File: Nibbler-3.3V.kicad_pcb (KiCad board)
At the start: 2 copper layers, 17.7 x 10.2 mm, 11 parts, among them J1 CONN_01X04, J2 +3.3, J3 GND, Q1 UM6K33N, Q2 UM6K33N

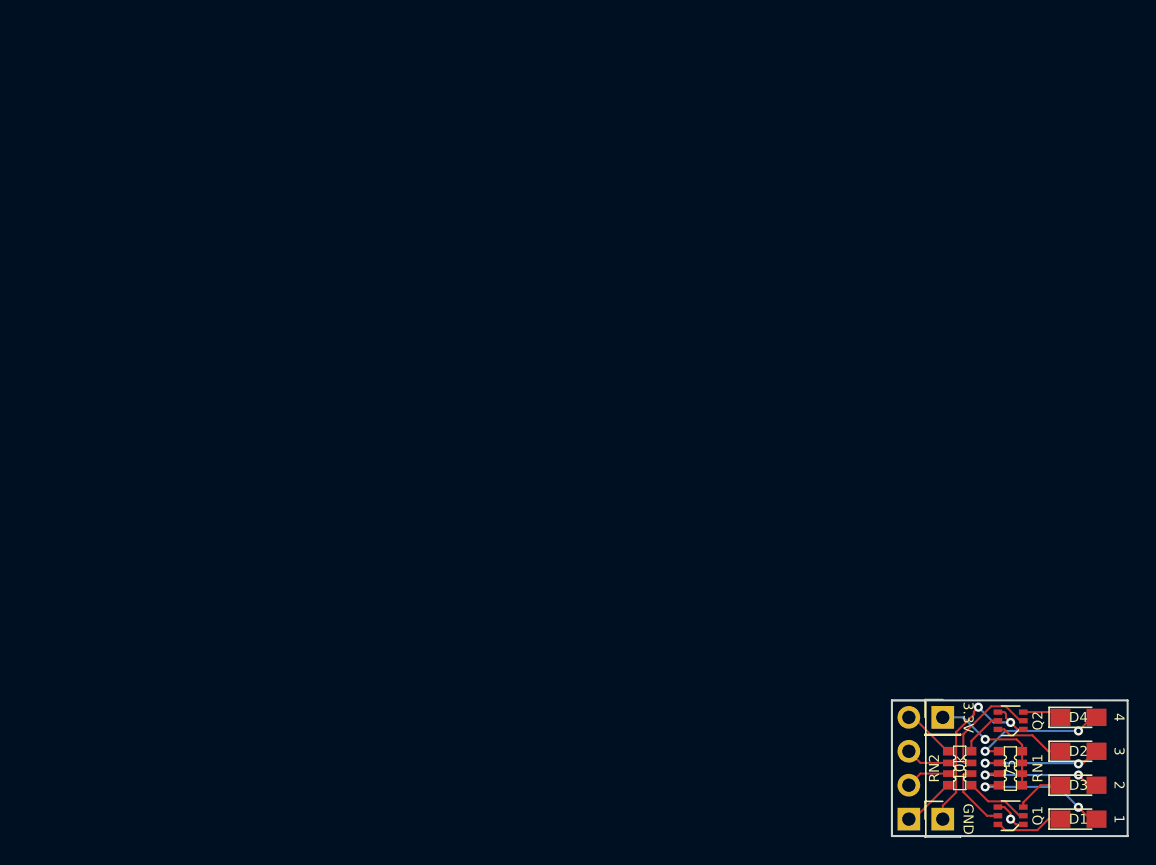
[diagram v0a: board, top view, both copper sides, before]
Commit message: Minor layout rework - rotated current limit resistor in layout and reversed LED connections in schematic. Modified bottom silkscreen text
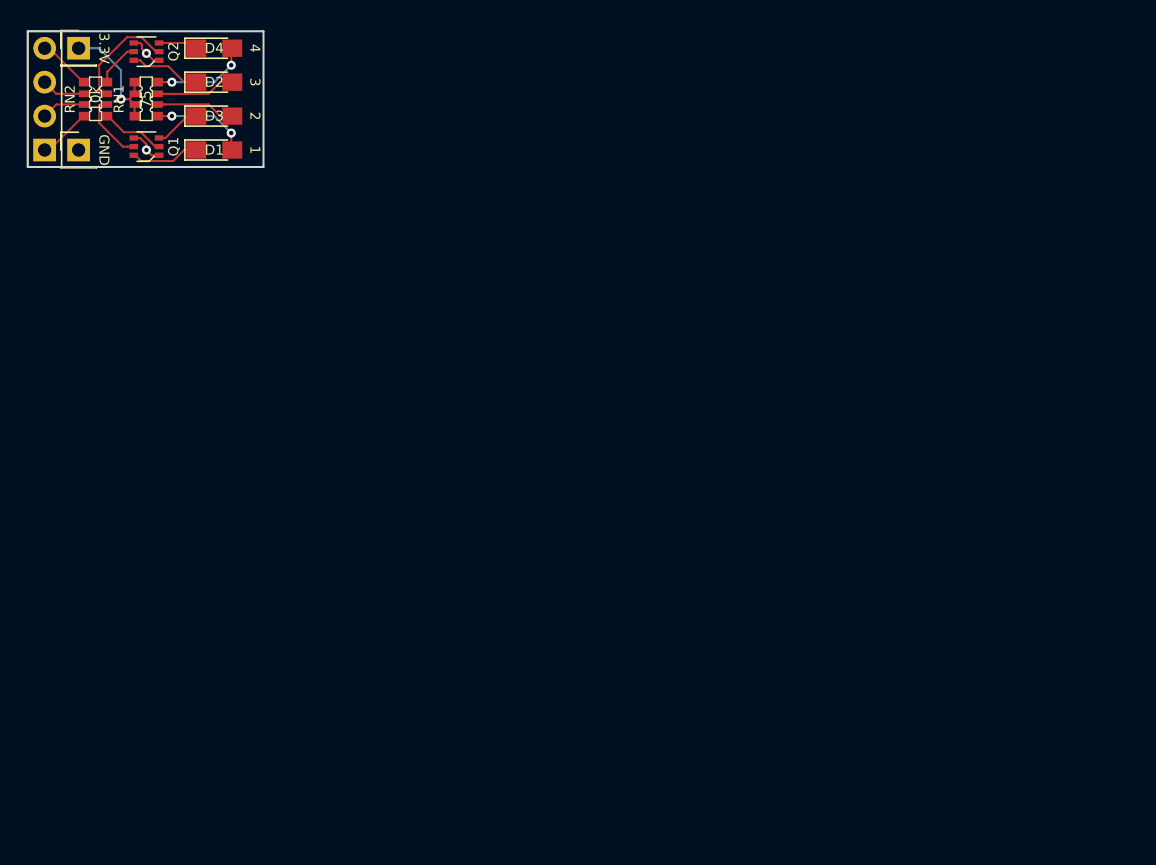
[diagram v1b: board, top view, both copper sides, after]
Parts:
- moved D1 81.8 mm to (96.7, 60.9)
- moved D2 81.8 mm to (96.7, 55.8)
- moved D3 81.8 mm to (96.7, 58.4)
- moved D4 81.8 mm to (96.7, 53.3)
- moved J1 81.8 mm to (84.0, 60.9)
- moved J2 81.8 mm to (86.6, 53.3)
- moved J3 81.8 mm to (86.6, 60.9)
- moved RN1 81.8 mm to (91.6, 57.1), turned to 0 degrees
- moved Q1 81.8 mm to (91.6, 60.6)
- moved Q2 81.8 mm to (91.6, 53.5)
- moved RN2 81.8 mm to (87.8, 57.1)
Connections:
- RN1 pad 5: /LED4 -> /LED1
- RN1 pad 6: /LED3 -> /LED2
- RN1 pad 7: /LED2 -> /LED3
- RN1 pad 8: /LED1 -> /LED4
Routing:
- net GNDREF: track 17.7 -> 5.31 mm, vias 3 -> 2
- net /LED2: track 9.71 -> 5.94 mm, vias 2 -> 0
- net /LED3: track 9.77 -> 6.04 mm, vias 2 -> 0
- net /LED4: track 10.5 -> 7.65 mm
- net /LED1: track 10.4 -> 7.78 mm
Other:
- board text added: "Jacob Miller 2017 v1.1 3.3 Volt"
- board text added: "Nibbler"
- board text removed: "3.3 Volt Jacob Miller v0.1 - 2017"
- board text removed: "Green Nibbler"
